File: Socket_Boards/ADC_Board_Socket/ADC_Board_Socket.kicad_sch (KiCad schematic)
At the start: 2 parts

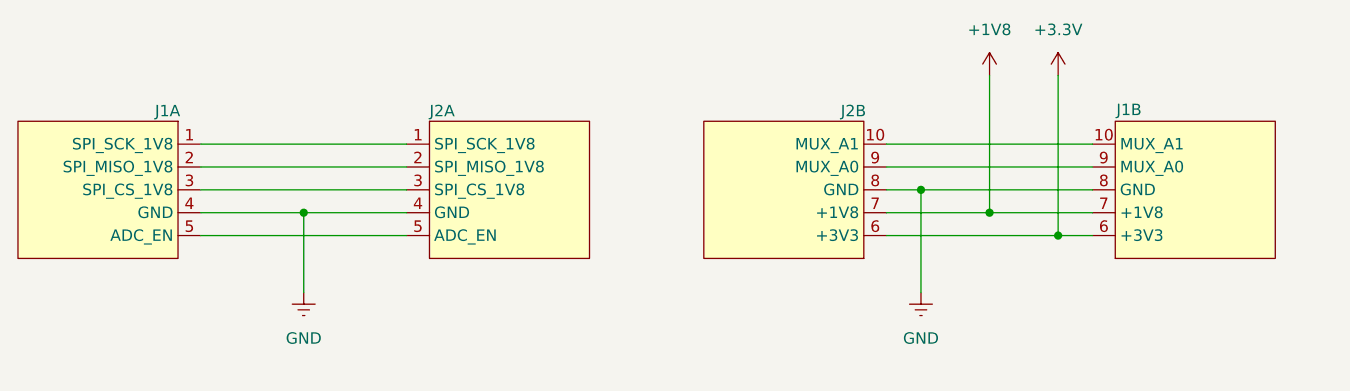
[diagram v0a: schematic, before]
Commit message: Fixed bugs. Added comments. Push before changing the ADC
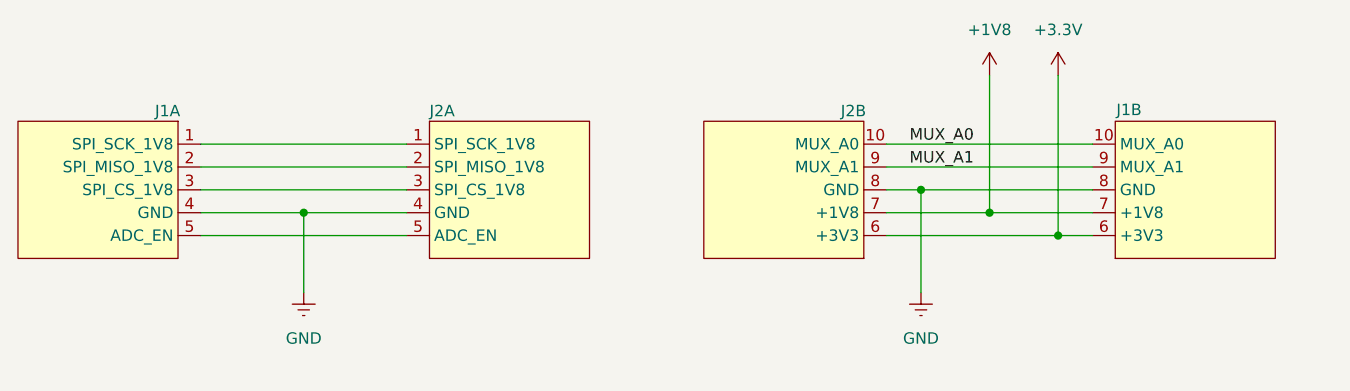
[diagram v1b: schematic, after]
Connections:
- net MUX_A0: now reaches J1.10 (MUX_A0), J2.10 (MUX_A0)
- net MUX_A1: now reaches J1.9 (MUX_A1), J2.9 (MUX_A1)
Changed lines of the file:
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@@
+		)
+	)
+	(label "MUX_A0"
+		(at 181.61 91.44 0)
+		(fields_autoplaced yes)
+		(effects
+			(font
+				(size 1.27 1.27)
+			)
+			(justify left bottom)
+		)
+	)
+	(label "MUX_A1"
+		(at 181.61 93.98 0)
+		(fields_autoplaced yes)
+		(effects
+			(font
+				(size 1.27 1.27)
+			)
+			(justify left bottom)
 		)
 	)
@@
 	)
 	(symbol
+		(lib_name "ADC_Board_Socket_Conn_1.27mm_1")
 		(lib_id "X-MODs_SchLib:ADC_Board_Socket_Conn_1.27mm")
 		(at 176.53 104.14 180)

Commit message: Added new version of the ADC Board. Better ADC, precision reference. Similar power consumption
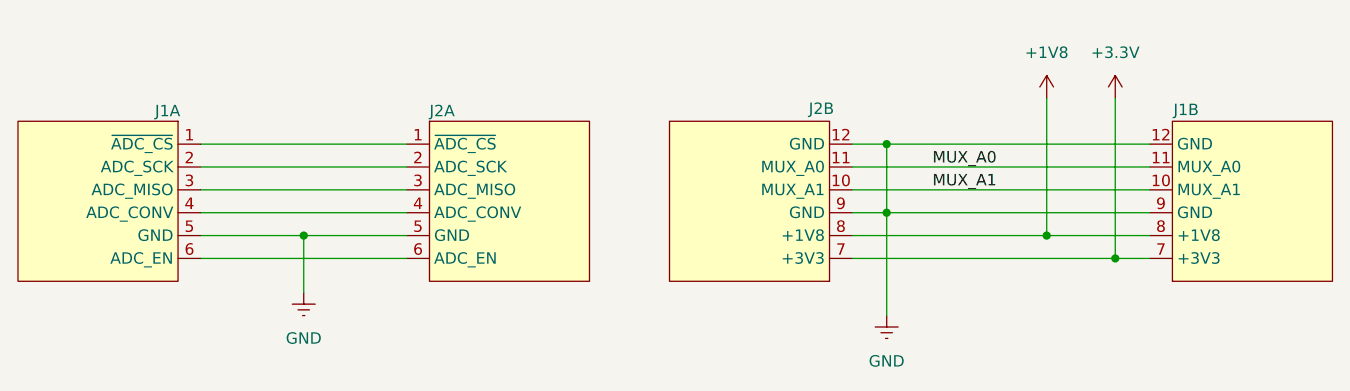
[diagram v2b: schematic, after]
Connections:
- net +1V8: now also J1.8 (+1V8), J2.8 (+1V8); no longer J1.7 (+1V8), J2.7 (+1V8)
- net +3.3V: now also J1.7 (+3V3), J2.7 (+3V3); no longer J1.6 (+3V3), J2.6 (+3V3)
- net GND: now also J1.12 (GND), J1.5 (GND), J1.9 (GND), J2.12 (GND), J2.5 (GND), J2.9 (GND); no longer J1.4 (GND), J1.8 (GND), J2.4 (GND), J2.8 (GND)
- net MUX_A0: now also J1.11 (MUX_A0), J2.11 (MUX_A0); no longer J1.10 (MUX_A0), J2.10 (MUX_A0)
- net MUX_A1: now also J1.10 (MUX_A1), J2.10 (MUX_A1); no longer J1.9 (MUX_A1), J2.9 (MUX_A1)
- new net: J1.4 (ADC_CONV), J2.4 (ADC_CONV)
- new net: J1.6 (ADC_EN), J2.6 (ADC_EN)
